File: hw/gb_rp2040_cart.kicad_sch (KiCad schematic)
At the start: 9 parts, among them J1 GameBoy_Cartridge, J2 DEBUG, Q1 Si2319CDS, SW1 RESET, U1 Pico

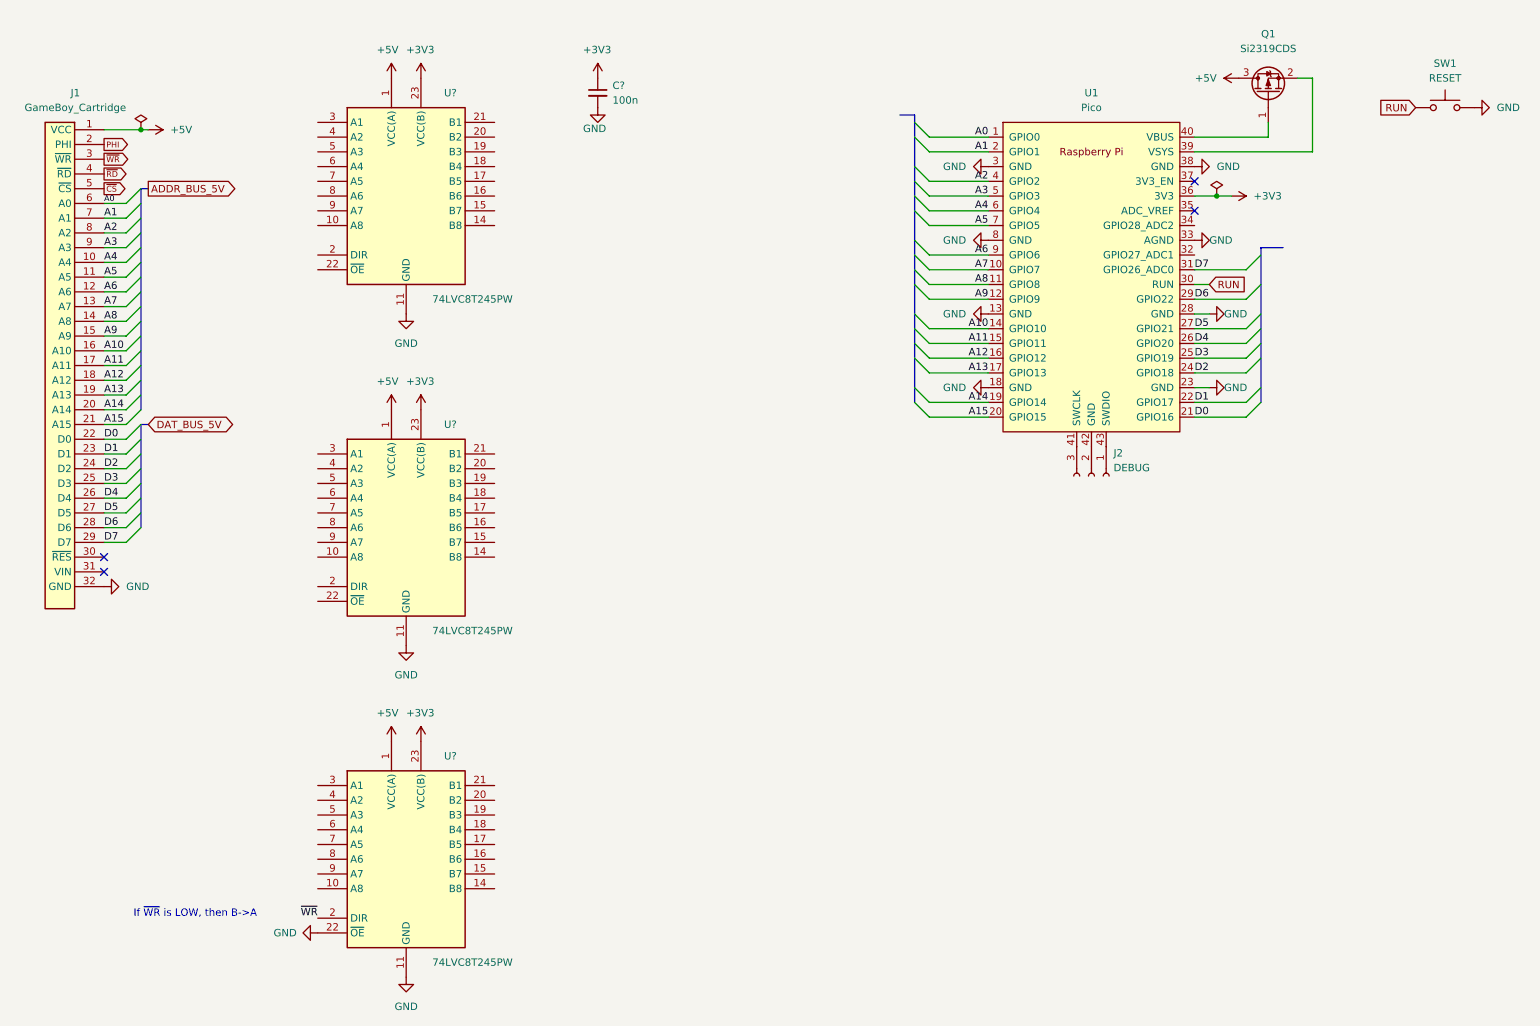
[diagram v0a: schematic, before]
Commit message: Finish schematic
Signed-off-by: Mahyar Koshkouei <mk@deltabeard.com>
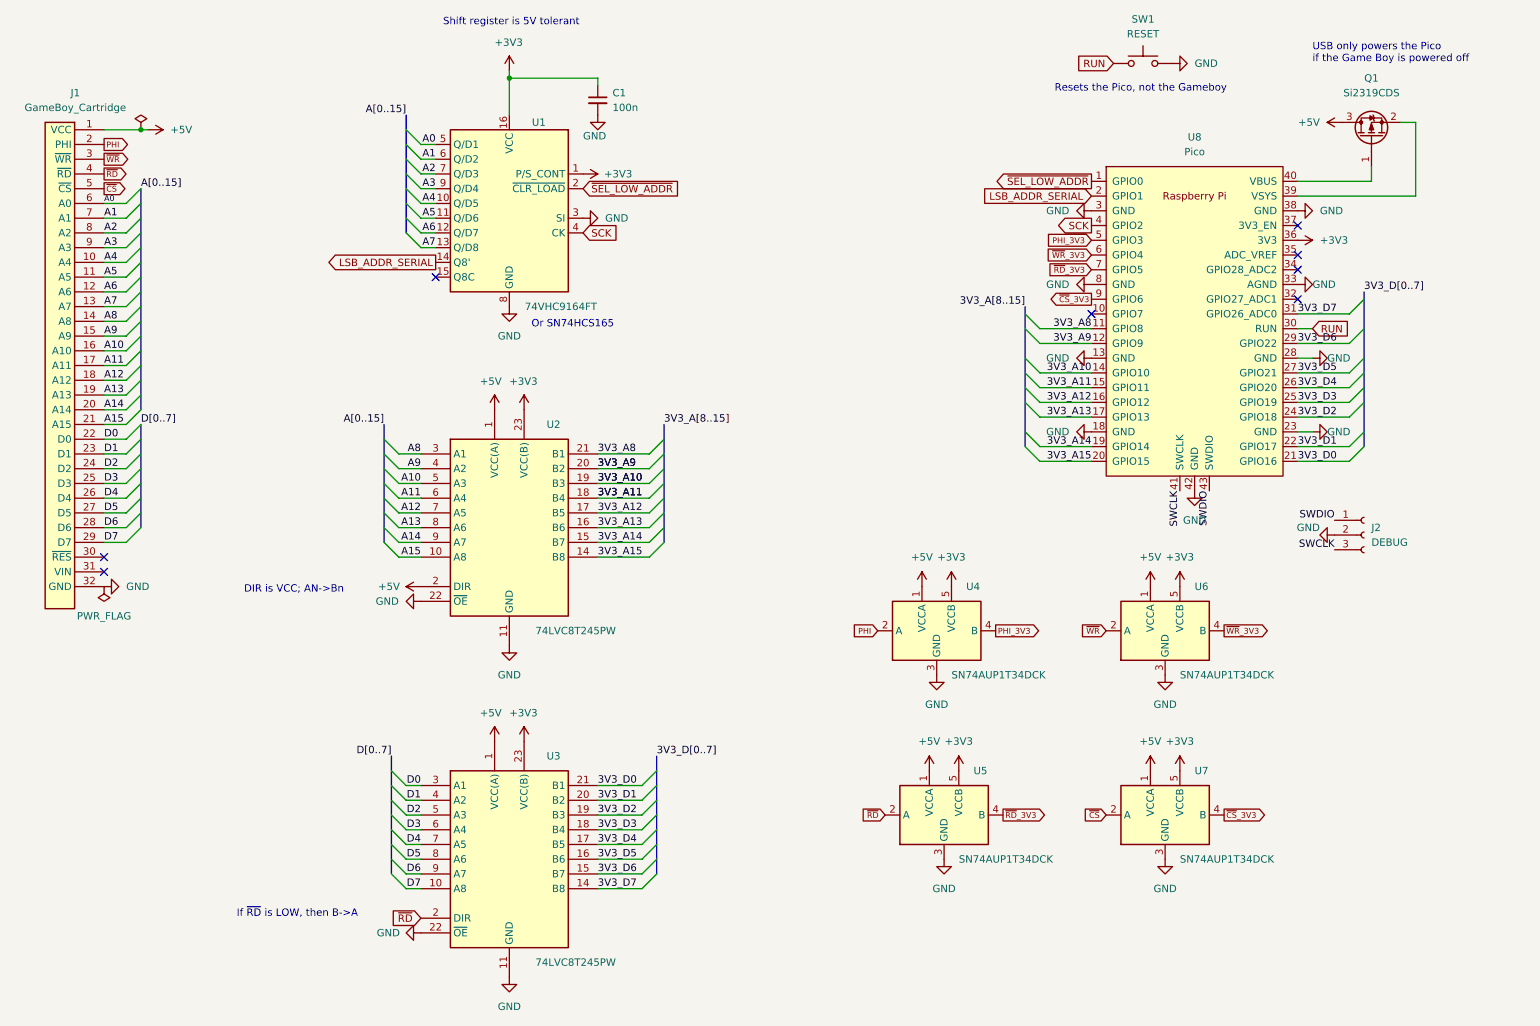
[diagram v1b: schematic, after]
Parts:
- removed U?: 74LVC8T245PW, Package_SO:TSSOP-24_4.4x7.8mm_P0.65mm, symbol Gekkio_Logic_LevelTranslator:74LVC8T245PW
- added U1: 74VHC9164FT, Package_SO:TSSOP-16_4.4x5mm_P0.65mm, symbol 74xx:74VHC9164FT
- added U4, U5, U6, U7: SN74AUP1T34DCK, Package_TO_SOT_SMD:SOT-353_SC-70-5, symbol Logic_LevelTranslator:SN74AUP1T34DCK
- C1: renamed from C?; footprint (none) -> Capacitor_SMD:C_0603_1608Metric
- J1: footprint (none) -> Gekkio_Connector_PCBEdge:GameBoy_Cartridge_1x32_P1.50mm_Edge
- J2: footprint (none) -> Connector_PinSocket_2.54mm:PinSocket_1x03_P2.54mm_Vertical_SMD_Pin1Left
- SW1: footprint (none) -> Button_Switch_SMD:SW_SPST_B3U-1000P-B
- U8: renamed from U1; footprint RPi_Pico:RPi_Pico_SMD_TH -> MCU_RaspberryPi_and_Boards:RPi_Pico_SMD_TH
- gave numbers to parts that had none: 2
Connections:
- net +3V3: now also U1.1 (P/S_CONT), U1.16 (VCC), U4.5 (VCCB), U5.5 (VCCB), U6.5 (VCCB), U7.5 (VCCB)
- net +5V: now also U2.2 (DIR), U4.1 (VCCA), U5.1 (VCCA), U6.1 (VCCA), U7.1 (VCCA)
- net A0: now also U1.5 (Q/D1); no longer U8.1 (GPIO0)
- net A1: now also U1.6 (Q/D2); no longer U8.2 (GPIO1)
- net A10: now also U2.5 (A3); no longer U8.14 (GPIO10)
- net A11: now also U2.6 (A4); no longer U8.15 (GPIO11)
- net A12: now also U2.7 (A5); no longer U8.16 (GPIO12)
- net A13: now also U2.8 (A6); no longer U8.17 (GPIO13)
- net A14: now also U2.9 (A7); no longer U8.19 (GPIO14)
- net A15: now also U2.10 (A8); no longer U8.20 (GPIO15)
- net A2: now also U1.7 (Q/D3); no longer U8.4 (GPIO2)
- net A3: now also U1.9 (Q/D4); no longer U8.5 (GPIO3)
- net A4: now also U1.10 (Q/D5); no longer U8.6 (GPIO4)
- net A5: now also U1.11 (Q/D6); no longer U8.7 (GPIO5)
- net A6: now also U1.12 (Q/D7); no longer U8.9 (GPIO6)
- net A7: now also U1.13 (Q/D8); no longer U8.10 (GPIO7)
- net A8: now also U2.3 (A1); no longer U8.11 (GPIO8)
- net A9: now also U2.4 (A2); no longer U8.12 (GPIO9)
- net D0: now also U3.3 (A1); no longer U8.21 (GPIO16)
- net D1: now also U3.4 (A2); no longer U8.22 (GPIO17)
- net D2: now also U3.5 (A3); no longer U8.24 (GPIO18)
- net D3: now also U3.6 (A4); no longer U8.25 (GPIO19)
- net D4: now also U3.7 (A5); no longer U8.26 (GPIO20)
- net D5: now also U3.8 (A6); no longer U8.27 (GPIO21)
- net D6: now also U3.9 (A7); no longer U8.29 (GPIO22)
- net D7: now also U3.10 (A8); no longer U8.31 (GPIO26_ADC0)
- net GND: now also J2.2 (Pin_2), U2.22 (~{OE}), U8.42 (GND), U1.3 (SI), U1.8 (GND), U4.3 (GND), U5.3 (GND), U6.3 (GND), U7.3 (GND)
- net PHI: now also U4.2 (A)
- net ~{CS}: now also U7.2 (A)
- net ~{RD}: now also U3.2 (DIR), U5.2 (A)
- net ~{WR}: now also U6.2 (A); no longer U3.2 (DIR)
- net SWCLK: now reaches J2.3 (Pin_3), U8.41 (SWCLK)
- net SWDIO: now reaches J2.1 (Pin_1), U8.43 (SWDIO)
- net 3V3_D7: now reaches U3.14 (B8)
- net 3V3_D7: now also U8.31 (GPIO26_ADC0)
- net 3V3_D6: now reaches U3.15 (B7)
- net 3V3_D6: now also U8.29 (GPIO22)
- net 3V3_D5: now reaches U3.16 (B6)
- net 3V3_D5: now also U8.27 (GPIO21)
- net 3V3_D4: now reaches U3.17 (B5)
- net 3V3_D4: now also U8.26 (GPIO20)
- net 3V3_D3: now reaches U3.18 (B4)
- net 3V3_D3: now also U8.25 (GPIO19)
- net 3V3_D2: now reaches U3.19 (B3)
- net 3V3_D2: now also U8.24 (GPIO18)
- net 3V3_D1: now reaches U3.20 (B2)
- net 3V3_D1: now also U8.22 (GPIO17)
- net 3V3_D0: now reaches U3.21 (B1)
- net 3V3_D0: now also U8.21 (GPIO16)
- net 3V3_A15: now reaches U2.14 (B8)
- net 3V3_A15: now also U8.20 (GPIO15)
- net 3V3_A14: now reaches U2.15 (B7)
- net 3V3_A14: now also U8.19 (GPIO14)
- net 3V3_A13: now reaches U2.16 (B6)
- net 3V3_A13: now also U8.17 (GPIO13)
- net 3V3_A12: now reaches U2.17 (B5)
- net 3V3_A12: now also U8.16 (GPIO12)
- net 3V3_A11: now reaches U2.18 (B4)
- net 3V3_A11: now also U8.15 (GPIO11)
- net 3V3_A10: now reaches U2.19 (B3)
- net 3V3_A10: now also U8.14 (GPIO10)
- net 3V3_A9: now reaches U2.20 (B2)
- net 3V3_A9: now also U8.12 (GPIO9)
- net 3V3_A8: now reaches U2.21 (B1)
- net 3V3_A8: now also U8.11 (GPIO8)
- new net LSB_ADDR_SERIAL: U1.14 (Q8'), U8.2 (GPIO1)
- new net PHI_3V3: U4.4 (B), U8.5 (GPIO3)
- new net SCK: U1.4 (CK), U8.4 (GPIO2)
- new net ~{CS}_3V3: U7.4 (B), U8.9 (GPIO6)
- new net ~{RD}_3V3: U5.4 (B), U8.7 (GPIO5)
- new net ~{SEL_LOW_ADDR}: U1.2 (~{CLR_LOAD}), U8.1 (GPIO0)
- new net ~{WR}_3V3: U6.4 (B), U8.6 (GPIO4)
- no-connect marks 4 -> 8
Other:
- note added: "DIR is VCC; AN->Bn"
- note added: "If ~{RD} is LOW, then B->A"
- note added: "Or SN74HCS165"
- note added: "Resets the Pico, not the Gameboy"
- note added: "Shift register is 5V tolerant"
- note added: "USB only powers the Pico if the Game Boy is powered off"
- note removed: "If ~{WR} is LOW, then B->A"
- moved on the sheet: C1, J2, Q1, SW1, U2, U3, U8

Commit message: Use RP2040 instead of Pico
Signed-off-by: Mahyar Koshkouei <mk@deltabeard.com>
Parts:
- added C? (x2): 1u, symbol Device:C_Small
- added D?: D_Schottky, symbol Device:D_Schottky
- added J?: USB_C_Receptacle_USB2.0, symbol Connector:USB_C_Receptacle_USB2.0
- added Q?: Si2319CDS, Package_TO_SOT_SMD:SOT-23, symbol Transistor_FET:Si2319CDS
- added R? (x2): 5k1, symbol Device:R_Small
- added R?: 10k, symbol Device:R_Small
- added R? (x2): 27.4R, symbol Device:R_Small
- added U?: RP2040, RP2040_minimal:RP2040-QFN-56, symbol RP_RP2040:RP2040
- added U?: TLV70233_WSON6, Package_SON:WSON-6_1.5x1.5mm_P0.5mm, symbol Regulator_Linear:TLV70233_WSON6
- added U?: W25Q128JVS, Package_SO:SOIC-8_5.23x5.23mm_P1.27mm, symbol Memory_Flash:W25Q128JVS
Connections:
- net +3V3: now also C?.1, U?.3 (OUT), U?.8 (VCC)
- net +5V: now also C?.1, D?.1 (K), Q?.2 (S), U?.1 (IN), U?.6 (EN); no longer J1.1 (VCC)
- net GND: now also C?.2, C?.2, J?.A1 (GND), J?.A12 (GND), J?.B1 (GND), J?.B12 (GND), J?.S1 (SHIELD), R?.1, R?.2, R?.2, U?.2 (GND), U?.4 (GND)
- new net: R?.1, U?.46 (USB_DM)
- new net: R?.1, U?.47 (USB_DP)
- new net: J?.B5 (CC2), R?.2
- new net: J?.A5 (CC1), R?.1
- new net GB_5V: J1.1 (VCC), Q?.3 (D)
- new net QSPI_SCLK: U?.52 (QSPI_SCLK), U?.6 (CLK)
- new net QSPI_SD0: U?.5 (DI(IO0)), U?.53 (QSPI_SD0)
- new net QSPI_SD1: U?.2 (DO(IO1)), U?.55 (QSPI_SD1)
- new net QSPI_SD2: U?.54 (QSPI_SD2), U?.7 (IO3)
- new net QSPI_SD3: U?.3 (IO2), U?.51 (QSPI_SD3)
- new net QSPI_SS: U?.1 (~{CS}), U?.56 (QSPI_SS)
- new net USB_DM: J?.A7 (D-), J?.B7 (D-), R?.2
- new net USB_DP: J?.A6 (D+), J?.B6 (D+), R?.2
- new net VBUS: D?.2 (A), J?.A4 (VBUS), J?.A9 (VBUS), J?.B4 (VBUS), J?.B9 (VBUS), Q?.1 (G), R?.1
- no-connect marks 8 -> 10

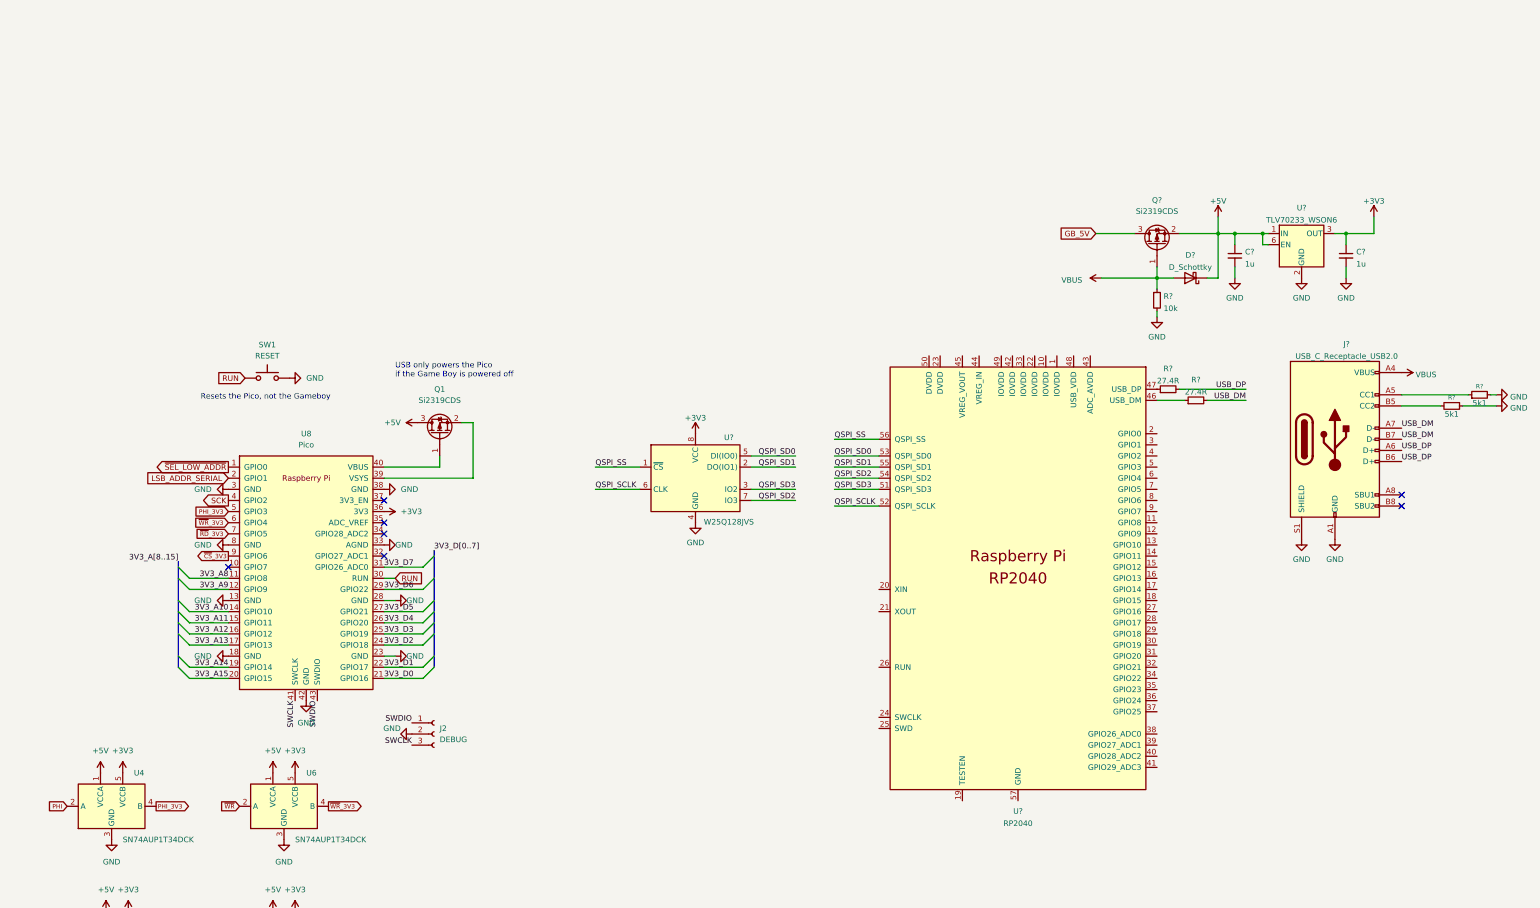
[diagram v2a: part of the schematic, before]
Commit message: hw: connect cart to RP2040
Signed-off-by: Mahyar Koshkouei <mk@deltabeard.com>
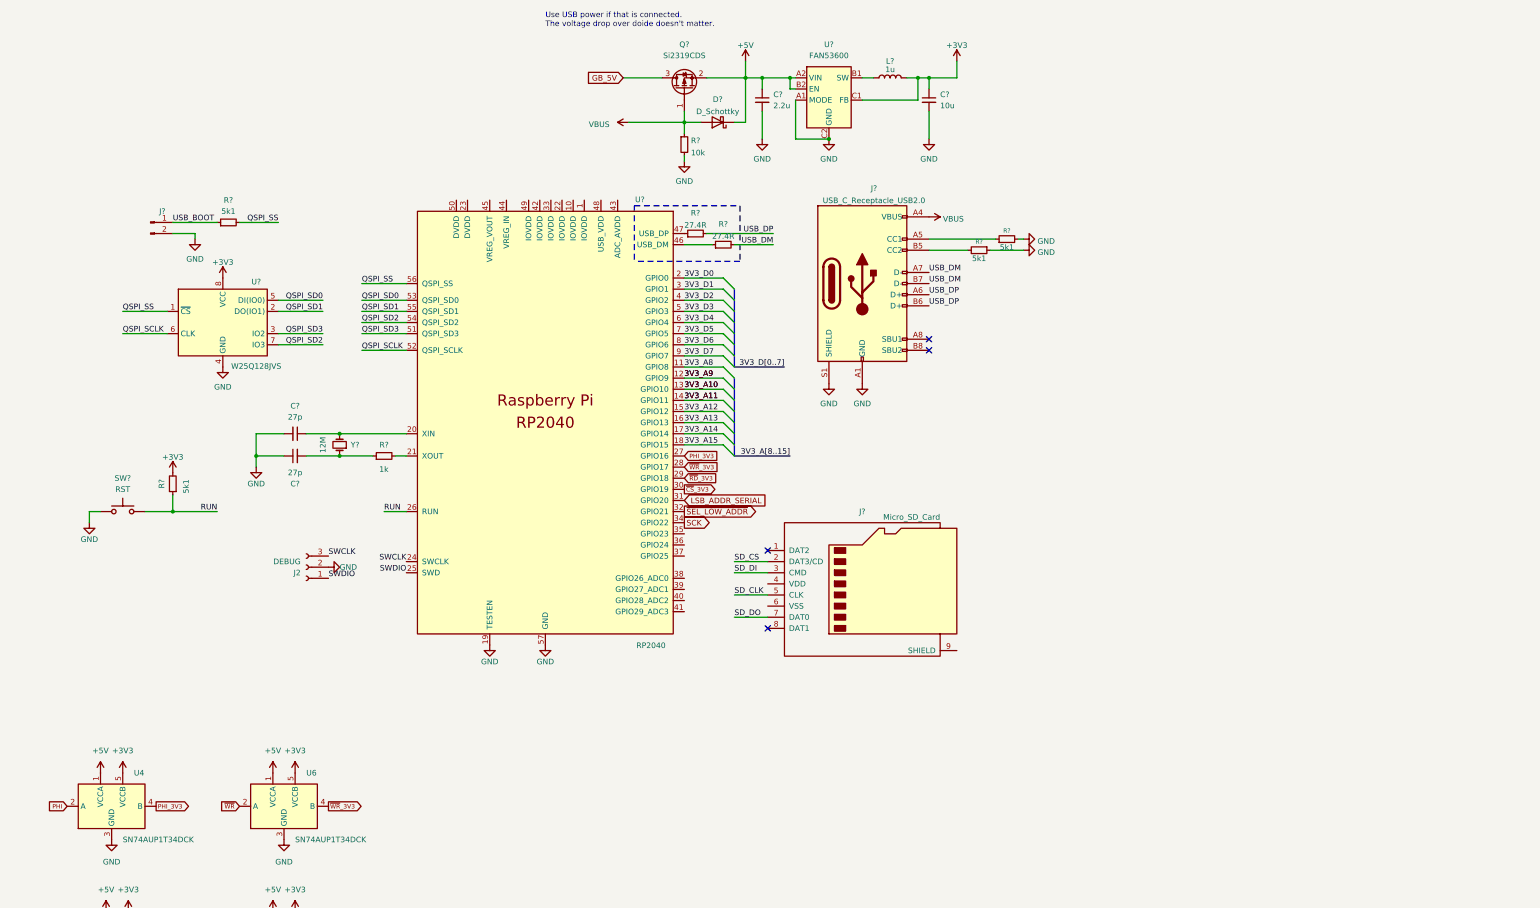
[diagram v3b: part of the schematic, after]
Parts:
- removed Q1: Si2319CDS, Package_TO_SOT_SMD:SOT-23, symbol Transistor_FET:Si2319CDS
- removed SW1: RESET, Button_Switch_SMD:SW_SPST_B3U-1000P-B, symbol Switch:SW_Push
- removed U8: Pico, MCU_RaspberryPi_and_Boards:RPi_Pico_SMD_TH, symbol MCU_RaspberryPi_and_Boards:Pico
- removed U?: TLV70233_WSON6, Package_SON:WSON-6_1.5x1.5mm_P0.5mm, symbol Regulator_Linear:TLV70233_WSON6
- added C? (x2): 27p, symbol Device:C_Small
- added J?: Micro_SD_Card, symbol Connector:Micro_SD_Card
- added J?: USB_BOOT, symbol Connector:Conn_01x02_Male
- added L?: 1u, symbol Device:L
- added R?: 1k, symbol Device:R_Small
- added R? (x2): 5k1, symbol Device:R_Small
- added SW?: RST, symbol Switch:SW_Push
- added U?: FAN53600, symbol Project_specific:FAN53600
- added Y?: 12M, symbol Device:Crystal_Small
- C?: value 1u -> 2.2u
- C?: value 1u -> 10u
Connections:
- net +3V3: now also L?.2, R?.2, U?.C1 (FB)
- net +5V: now also U?.A2 (VIN), U?.B2 (EN)
- net 3V3_A10: now also U?.13 (GPIO10)
- net 3V3_A11: now also U?.14 (GPIO11)
- net 3V3_A12: now also U?.15 (GPIO12)
- net 3V3_A13: now also U?.16 (GPIO13)
- net 3V3_A14: now also U?.17 (GPIO14)
- net 3V3_A15: now also U?.18 (GPIO15)
- net 3V3_A8: now also U?.11 (GPIO8)
- net 3V3_A9: now also U?.12 (GPIO9)
- net 3V3_D0: now also U?.2 (GPIO0)
- net 3V3_D1: now also U?.3 (GPIO1)
- net 3V3_D2: now also U?.4 (GPIO2)
- net 3V3_D3: now also U?.5 (GPIO3)
- net 3V3_D4: now also U?.6 (GPIO4)
- net 3V3_D5: now also U?.7 (GPIO5)
- net 3V3_D6: now also U?.8 (GPIO6)
- net 3V3_D7: now also U?.9 (GPIO7)
- net GND: now also U?.19 (TESTEN), U?.57 (GND), C?.1, C?.2, J?.2 (Pin_2), SW?.1, U?.A1 (MODE), U?.C2 (GND)
- net LSB_ADDR_SERIAL: now also U?.31 (GPIO20)
- net PHI_3V3: now also U?.27 (GPIO16)
- net QSPI_SS: now also R?.2
- net RUN: now also U?.26 (RUN), R?.1, SW?.2
- net SCK: now also U?.34 (GPIO22)
- net SWCLK: now also U?.24 (SWCLK)
- net SWDIO: now also U?.25 (SWD)
- net ~{CS}_3V3: now also U?.30 (GPIO19)
- net ~{RD}_3V3: now also U?.29 (GPIO18)
- net ~{SEL_LOW_ADDR}: now also U?.32 (GPIO21)
- net ~{WR}_3V3: now also U?.28 (GPIO17)
- net at U?.20 (XIN): now also C?.1, Y?.2
- net at U?.21 (XOUT): now also R?.2
- new net: C?.2, R?.1, Y?.1
- new net: L?.1, U?.B1 (SW)
- new net SD_CLK: J?.5 (CLK)
- new net SD_CS: J?.2 (DAT3/CD)
- new net SD_DI: J?.3 (CMD)
- new net SD_DO: J?.7 (DAT0)
- new net USB_BOOT: J?.1 (Pin_1), R?.1
- no-connect marks 10 -> 7
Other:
- note added: "Use USB power if that is connected. The voltage drop over doide doesn't matter."
- note removed: "Resets the Pico, not the Gameboy"
- note removed: "USB only powers the Pico if the Game Boy is powered off"
- moved on the sheet: C?, D?, J2, J?, Q?, R?, U?
